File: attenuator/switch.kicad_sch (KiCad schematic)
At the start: 4 parts, among them U1 4259-63

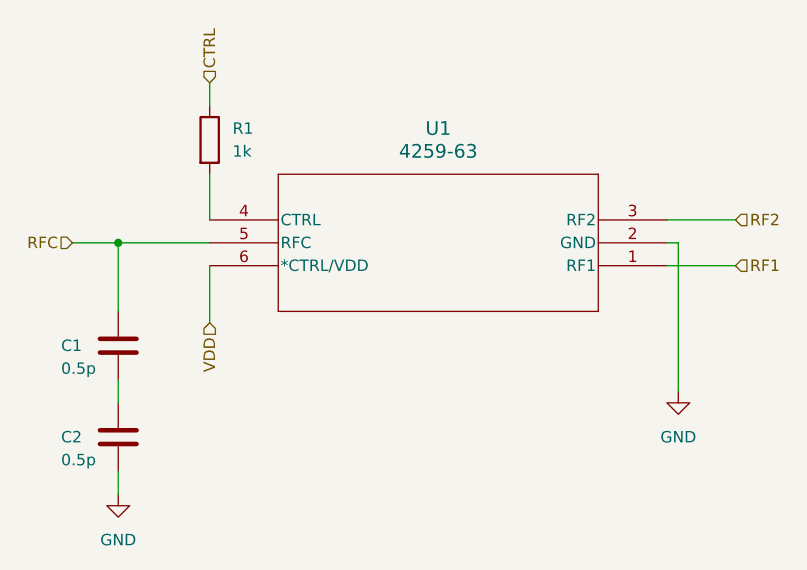
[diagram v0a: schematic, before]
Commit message: change hierarchical sheets
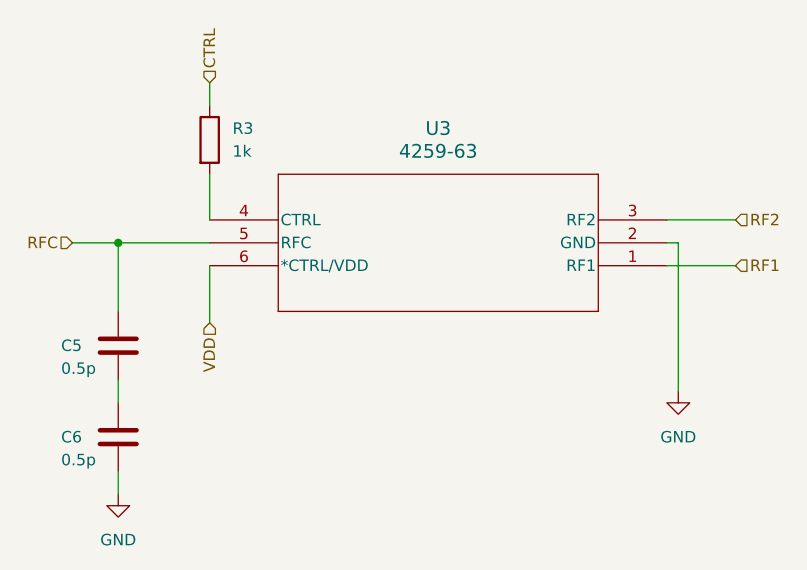
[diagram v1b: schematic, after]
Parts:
- renumbered C1 to C5, C2 to C6, R1 to R3, U1 to U3
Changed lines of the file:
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@@
   (symbol (lib_id "Device:C") (at 114.3 100.33 0) (unit 1)
     (in_bom yes) (on_board yes) (dnp no)
-    (property "Reference" "C1" (at 107.95 100.33 0)
+    (property "Reference" "C5" (at 107.95 100.33 0)
       (effects (font (size 1.27 1.27)) (justify left))
     )
@@
     (instances
       (project "attenuator"
-        (path "/3b0f5433-415e-45c9-9c4a-85a692e565e5/0a76be8f-668a-4165-96ab-60e35cd849cd"
-          (reference "C1") (unit 1)
-        )
-        (path "/3b0f5433-415e-45c9-9c4a-85a692e565e5/169b8f2b-0aa0-4759-8e65-ab1053e64003"
-          (reference "C3") (unit 1)
-        )
         (path "/3b0f5433-415e-45c9-9c4a-85a692e565e5/30973910-c2d7-403a-a6fe-635552904991"
           (reference "C5") (unit 1)
@@
   (symbol (lib_id "rf_switch:4259-63") (at 175.26 91.44 180) (unit 1)
     (in_bom yes) (on_board yes) (dnp no) (fields_autoplaced)
-    (property "Reference" "U1" (at 149.86 76.2 0)
+    (property "Reference" "U3" (at 149.86 76.2 0)
       (effects (font (size 1.524 1.524)))
     )
@@
     (instances
       (project "attenuator"
-        (path "/3b0f5433-415e-45c9-9c4a-85a692e565e5/0a76be8f-668a-4165-96ab-60e35cd849cd"
-          (reference "U1") (unit 1)
-        )
-        (path "/3b0f5433-415e-45c9-9c4a-85a692e565e5/169b8f2b-0aa0-4759-8e65-ab1053e64003"
-          (reference "U2") (unit 1)
-        )
         (path "/3b0f5433-415e-45c9-9c4a-85a692e565e5/30973910-c2d7-403a-a6fe-635552904991"
           (reference "U3") (unit 1)
@@
   (symbol (lib_id "Device:R") (at 124.46 77.47 0) (unit 1)
     (in_bom yes) (on_board yes) (dnp no) (fields_autoplaced)
-    (property "Reference" "R1" (at 127 76.2 0)
+    (property "Reference" "R3" (at 127 76.2 0)
       (effects (font (size 1.27 1.27)) (justify left))
     )
@@
     (instances
       (project "attenuator"
-        (path "/3b0f5433-415e-45c9-9c4a-85a692e565e5/0a76be8f-668a-4165-96ab-60e35cd849cd"
-          (reference "R1") (unit 1)
-        )
-        (path "/3b0f5433-415e-45c9-9c4a-85a692e565e5/169b8f2b-0aa0-4759-8e65-ab1053e64003"
-          (reference "R2") (unit 1)
-        )
         (path "/3b0f5433-415e-45c9-9c4a-85a692e565e5/30973910-c2d7-403a-a6fe-635552904991"
           (reference "R3") (unit 1)
@@
   (symbol (lib_id "power:GND") (at 114.3 116.84 0) (unit 1)
     (in_bom yes) (on_board yes) (dnp no) (fields_autoplaced)
-    (property "Reference" "#PWR011" (at 114.3 123.19 0)
+    (property "Reference" "#PWR015" (at 114.3 123.19 0)
       (effects (font (size 1.27 1.27)) hide)
     )
@@
     (instances
       (project "attenuator"
-        (path "/3b0f5433-415e-45c9-9c4a-85a692e565e5/0a76be8f-668a-4165-96ab-60e35cd849cd"
-          (reference "#PWR011") (unit 1)
-        )
-        (path "/3b0f5433-415e-45c9-9c4a-85a692e565e5/169b8f2b-0aa0-4759-8e65-ab1053e64003"
-          (reference "#PWR013") (unit 1)
-        )
         (path "/3b0f5433-415e-45c9-9c4a-85a692e565e5/30973910-c2d7-403a-a6fe-635552904991"
           (reference "#PWR015") (unit 1)
@@
   (symbol (lib_id "power:GND") (at 176.53 105.41 0) (unit 1)
     (in_bom yes) (on_board yes) (dnp no) (fields_autoplaced)
-    (property "Reference" "#PWR012" (at 176.53 111.76 0)
+    (property "Reference" "#PWR016" (at 176.53 111.76 0)
       (effects (font (size 1.27 1.27)) hide)
     )
@@
     (instances
       (project "attenuator"
-        (path "/3b0f5433-415e-45c9-9c4a-85a692e565e5/0a76be8f-668a-4165-96ab-60e35cd849cd"
-          (reference "#PWR012") (unit 1)
-        )
-        (path "/3b0f5433-415e-45c9-9c4a-85a692e565e5/169b8f2b-0aa0-4759-8e65-ab1053e64003"
-          (reference "#PWR014") (unit 1)
-        )
         (path "/3b0f5433-415e-45c9-9c4a-85a692e565e5/30973910-c2d7-403a-a6fe-635552904991"
           (reference "#PWR016") (unit 1)
@@
   (symbol (lib_id "Device:C") (at 114.3 110.49 0) (unit 1)
     (in_bom yes) (on_board yes) (dnp no)
-    (property "Reference" "C2" (at 107.95 110.49 0)
+    (property "Reference" "C6" (at 107.95 110.49 0)
       (effects (font (size 1.27 1.27)) (justify left))
     )
@@
     (instances
       (project "attenuator"
-        (path "/3b0f5433-415e-45c9-9c4a-85a692e565e5/0a76be8f-668a-4165-96ab-60e35cd849cd"
-          (reference "C2") (unit 1)
-        )
-        (path "/3b0f5433-415e-45c9-9c4a-85a692e565e5/169b8f2b-0aa0-4759-8e65-ab1053e64003"
-          (reference "C4") (unit 1)
-        )
         (path "/3b0f5433-415e-45c9-9c4a-85a692e565e5/30973910-c2d7-403a-a6fe-635552904991"
           (reference "C6") (unit 1)
